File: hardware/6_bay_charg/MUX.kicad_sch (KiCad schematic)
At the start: 1 part, among them U6 TCA9548APWR

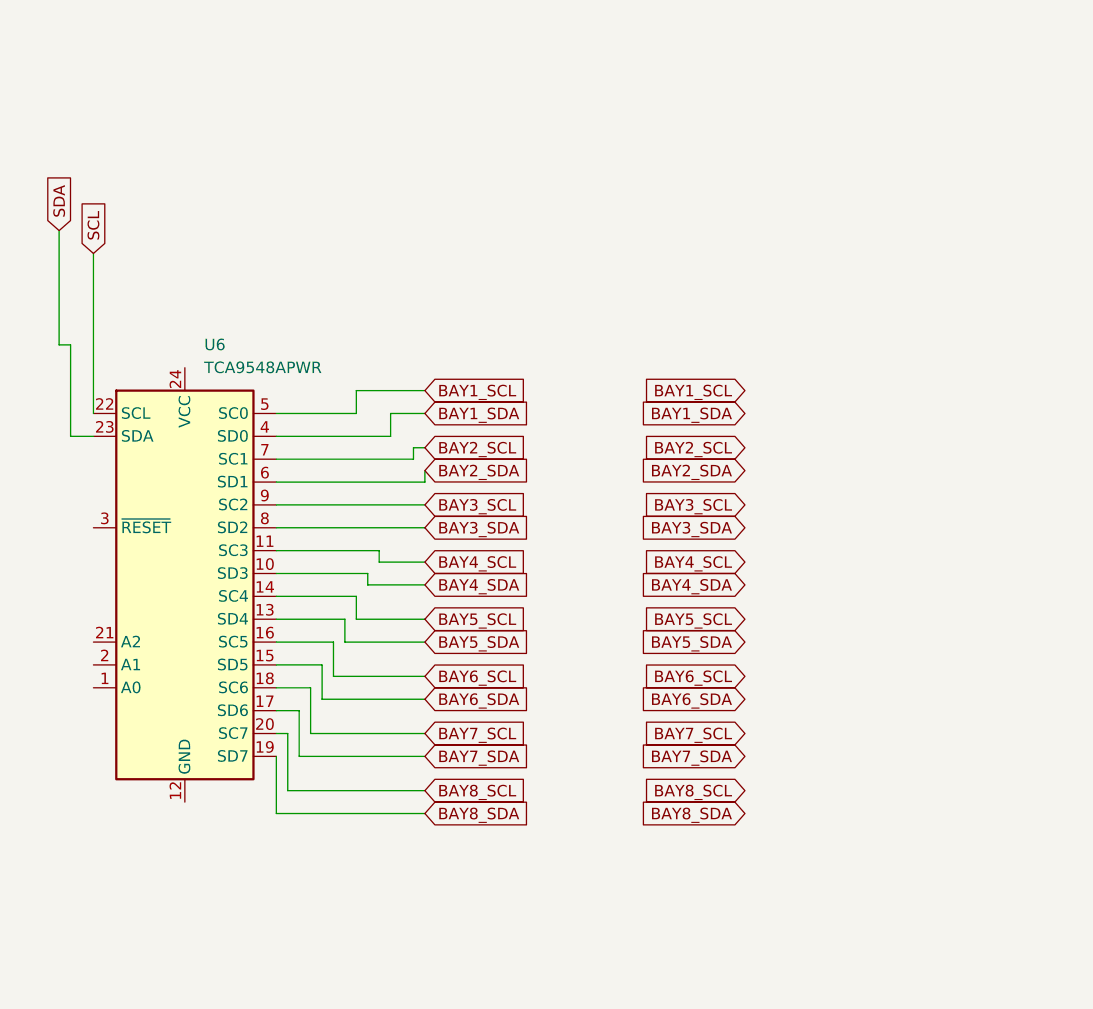
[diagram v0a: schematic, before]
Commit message: Update KiCad schematics: dual GPIO charge/discharge per bay
- Refactored bay power control logic
- Separated GPIOs for charge and discharge paths
- Added safe idle state with hardware interlock
- Improved overall safety and control clarity
- Updated and exported schematic PDF plots
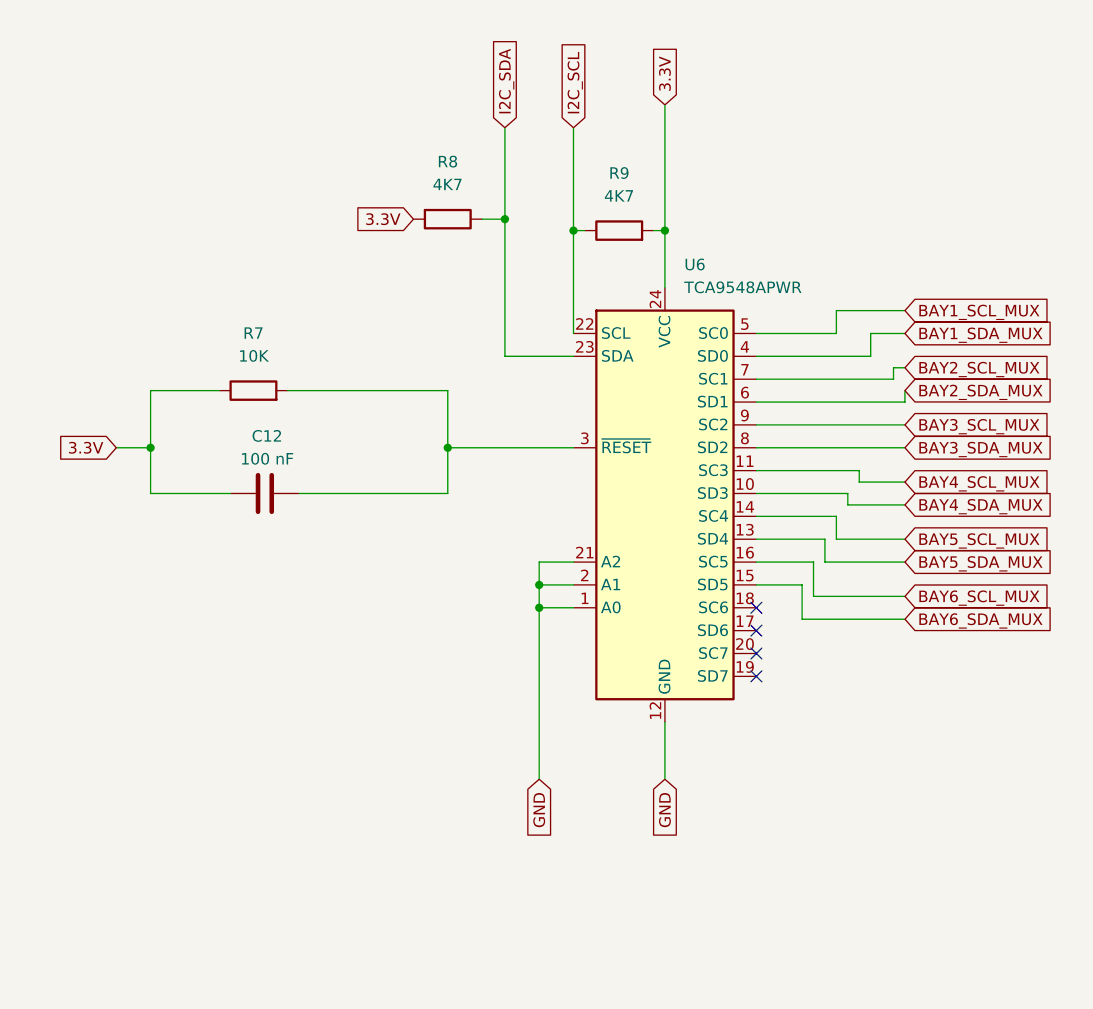
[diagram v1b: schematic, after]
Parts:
- added C12: 100 nF, symbol Device:C
- added R7: 10K, symbol Device:R
- added R8, R9: 4K7, symbol Device:R
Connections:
- net GND: now reaches U6.1 (A0)
- net GND: now also U6.12 (GND), U6.2 (A1), U6.21 (A2)
- net 3.3V: now reaches U6.24 (VCC)
- net 3.3V: now also C12.1, R7.1, R8.2, R9.2
- net at U6.3 (~{RESET}): now also C12.2, R7.2
- net BAY1_SCL renamed BAY1_SCL_MUX
- net BAY1_SDA renamed BAY1_SDA_MUX
- net BAY2_SCL renamed BAY2_SCL_MUX
- net BAY2_SDA renamed BAY2_SDA_MUX
- net BAY3_SCL renamed BAY3_SCL_MUX
- net BAY3_SDA renamed BAY3_SDA_MUX
- net BAY4_SCL renamed BAY4_SCL_MUX
- net BAY4_SDA renamed BAY4_SDA_MUX
- net BAY5_SCL renamed BAY5_SCL_MUX
- net BAY5_SDA renamed BAY5_SDA_MUX
- net BAY6_SCL renamed BAY6_SCL_MUX
- net BAY6_SDA renamed BAY6_SDA_MUX
- net BAY7_SCL: no longer names the net of U6.18 (SC6)
- net BAY7_SDA: no longer names the net of U6.17 (SD6)
- net BAY8_SCL: no longer names the net of U6.20 (SC7)
- net BAY8_SDA: no longer names the net of U6.19 (SD7)
- net SCL renamed I2C_SCL
- net I2C_SCL: now also R9.1
- net SDA renamed I2C_SDA
- net I2C_SDA: now also R8.1
- no-connect marks 0 -> 4
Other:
- title: (none) -> MUX
- moved on the sheet: U6

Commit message: Integrate fan, USB interface, firmware, and cleaned KiCad schematics
- Added 12V fan for thermal management
- Integrated USB interface (hardware and firmware)
- Added initial firmware implementation
- Cleaned and refactored KiCad schematics
- Updated and regenerated schematic PDF plots
- Updated project README to reflect latest architecture
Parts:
- R8, R9: value 4K7 -> 2K2
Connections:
- net 3.3V renamed +3.3V
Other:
- moved on the sheet: R8

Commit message: updating FSM diagramme
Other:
- note added: "MUX"
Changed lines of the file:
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@@
 		(comment 3 "Drawn by: Takiyeddin Gherras")
+	)
+	(text "MUX"
+		(exclude_from_sim no)
+		(at 147.32 148.59 0)
+		(effects
+			(font
+				(size 3.27 3.27)
+				(thickness 0.4088)
+			)
+		)
 	)
 	(junction
